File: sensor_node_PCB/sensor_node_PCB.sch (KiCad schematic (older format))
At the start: 32 parts, among them J1 USB_B_Mini, J3 OUTPUT_CONNECTOR, P1 BREAKOUTS, Q1 FDN340P, Q2 BSS138, Q3 BSS138, U1 LMV358IDGKR, U2 LD1117S50TR, U3 FT231XS, U4 LM1117-3.3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

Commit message: added dps310 to schem and board
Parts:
- added U?: dps310, symbol Kicad_symbols:dps310
- U9: symbol Kicad_symbols:sht20 -> sensor_node_PCB-rescue:sht20-Kicad_symbols
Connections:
- net 3V3_LDO: now also U9.~ (Vss), U?.6 (VDDIO), U?.8 (VDD); no longer U9.5 (VDD)
- net ARD_SCL_3V3: now also U9.~ (Vss), U?.4 (SCK); no longer U9.6 (SCL)
- net ARD_SDA_3V3: now also U9.~ (Vss), U?.3 (SDI); no longer U9.1 (SDA)
- net GND: now also U9.~ (Vss), U?.1 (GND), U?.7 (GND); no longer U9.2 (Vss)
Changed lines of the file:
@@
 	1350 1575 1675 1575
 $Comp
-L Kicad_symbols:sht20 U9
+L sensor_node_PCB-rescue:sht20-Kicad_symbols U9
 U 1 1 5FE5F04C
-P 7175 5275
-F 0 "U9" H 7000 5490 50  0000 C CNN
-F 1 "sht20" H 7000 5399 50  0000 C CNN
-F 2 "Package_DFN_QFN:DFN-6-1EP_3x3mm_P1mm_EP1.5x2.4mm" H 7175 5275 50  0001 C CNN
-F 3 "" H 7175 5275 50  0001 C CNN
-	1    7175 5275
+P 7275 5050
+F 0 "U9" H 7100 5355 50  0000 C CNN
+F 1 "sht20" H 7100 5264 50  0000 C CNN
+F 2 "Package_DFN_QFN:DFN-6-1EP_3x3mm_P1mm_EP1.5x2.4mm" H 7100 5173 50  0000 C CNN
+F 3 "" H 7275 5050 50  0001 C CNN
+	1    7275 5050
 	1    0    0    -1
 $EndComp
-Text Label 6500 5325 2    50   ~ 0
+Text Label 6600 5100 2    50   ~ 0
 ARD_SDA_3V3
-Text Label 7475 5325 0    50   ~ 0
+Text Label 7575 5100 0    50   ~ 0
 ARD_SCL_3V3
 $Comp
 L Arduino_Uno_R3_From_Scratch-rescue:3V3_LDO #PWR0113
 U 1 1 5FE707C4
-P 8050 5200
-F 0 "#PWR0113" H 8050 5160 30  0001 C CNN
-F 1 "3V3_LDO" H 8059 5338 30  0000 C CNN
-F 2 "" H 8050 5200 60  0000 C CNN
-F 3 "" H 8050 5200 60  0000 C CNN
-	1    8050 5200
+P 8150 4975
+F 0 "#PWR0113" H 8150 4935 30  0001 C CNN
+F 1 "3V3_LDO" H 8159 5113 30  0000 C CNN
+F 2 "" H 8150 4975 60  0000 C CNN
+F 3 "" H 8150 4975 60  0000 C CNN
+	1    8150 4975
 	1    0    0    -1
 $EndComp
@@
 L Arduino_Uno_R3_From_Scratch-rescue:GND #PWR0115
 U 1 1 5FE73051
-P 6425 5625
-F 0 "#PWR0115" H 6425 5375 50  0001 C CNN
-F 1 "GND" H 6430 5452 50  0000 C CNN
-F 2 "" H 6425 5625 60  0000 C CNN
-F 3 "" H 6425 5625 60  0000 C CNN
-	1    6425 5625
+P 6525 5400
+F 0 "#PWR0115" H 6525 5150 50  0001 C CNN
+F 1 "GND" H 6530 5227 50  0000 C CNN
+F 2 "" H 6525 5400 60  0000 C CNN
+F 3 "" H 6525 5400 60  0000 C CNN
+	1    6525 5400
 	1    0    0    -1
 $EndComp
 Wire Wire Line
-	6425 5625 6425 5425
+	6525 5400 6525 5200
 Wire Wire Line
-	6425 5425 6625 5425
+	6525 5200 6725 5200
 Wire Wire Line
-	7375 5325 7475 5325
+	7475 5100 7575 5100
 Wire Wire Line
-	6625 5325 6500 5325
+	6725 5100 6600 5100
 Wire Wire Line
-	8050 5200 8050 5425
+	8150 4975 8150 5200
 Wire Wire Line
-	8050 5425 7375 5425
+	8150 5200 7475 5200
+$Comp
+L Kicad_symbols:dps310 U?
+U 1 1 5FE12569
+P 7125 5925
+F 0 "U?" H 7125 6100 50  0000 C CNN
+F 1 "dps310" H 7125 6009 50  0000 C CNN
+F 2 "" H 7125 5925 50  0001 C CNN
+F 3 "" H 7125 5925 50  0001 C CNN
+	1    7125 5925
+	1    0    0    -1
+$EndComp
+$Comp
+L Arduino_Uno_R3_From_Scratch-rescue:GND #PWR?
+U 1 1 5FE1A61C
+P 6325 6000
+F 0 "#PWR?" H 6325 5750 50  0001 C CNN
+F 1 "GND" H 6330 5827 50  0000 C CNN
+F 2 "" H 6325 6000 60  0000 C CNN
+F 3 "" H 6325 6000 60  0000 C CNN
+	1    6325 6000
+	1    0    0    -1
+$EndComp
+Wire Wire Line
+	6325 6000 6325 5975
+Wire Wire Line
+	6325 5975 6675 5975
+$Comp
+L Arduino_Uno_R3_From_Scratch-rescue:GND #PWR?
+U 1 1 5FE23F96
+P 7875 6175
+F 0 "#PWR?" H 7875 5925 50  0001 C CNN
+F 1 "GND" H 7880 6002 50  0000 C CNN
+F 2 "" H 7875 6175 60  0000 C CNN
+F 3 "" H 7875 6175 60  0000 C CNN
+	1    7875 6175
+	0    -1   -1   0
+$EndComp
+Wire Wire Line
+	7575 6175 7875 6175
+$Comp
+L Arduino_Uno_R3_From_Scratch-rescue:3V3_LDO #PWR?
+U 1 1 5FE2D476
+P 8300 6000
+F 0 "#PWR?" H 8300 5960 30  0001 C CNN
+F 1 "3V3_LDO" H 8309 6138 30  0000 C CNN
+F 2 "" H 8300 6000 60  0000 C CNN
+F 3 "" H 8300 6000 60  0000 C CNN
+	1    8300 6000
+	1    0    0    -1
+$EndComp
+Wire Wire Line
+	7575 6275 8300 6275
+Wire Wire Line
+	7575 6075 8300 6075
+Wire Wire Line
+	8300 6075 8300 6000
+Wire Wire Line
+	8300 6075 8300 6275
+Connection ~ 8300 6075
+Text Label 6250 6400 2    50   ~ 0
+ARD_SDA_3V3
+Text Label 6250 6525 2    50   ~ 0
+ARD_SCL_3V3
+Wire Wire Line
+	6250 6400 6500 6400
+Wire Wire Line
+	6500 6400 6500 6175
+Wire Wire Line
+	6500 6175 6675 6175
+Wire Wire Line
+	6250 6525 6575 6525
+Wire Wire Line
+	6575 6525 6575 6275
+Wire Wire Line
+	6575 6275 6675 6275
 $EndSCHEMATC

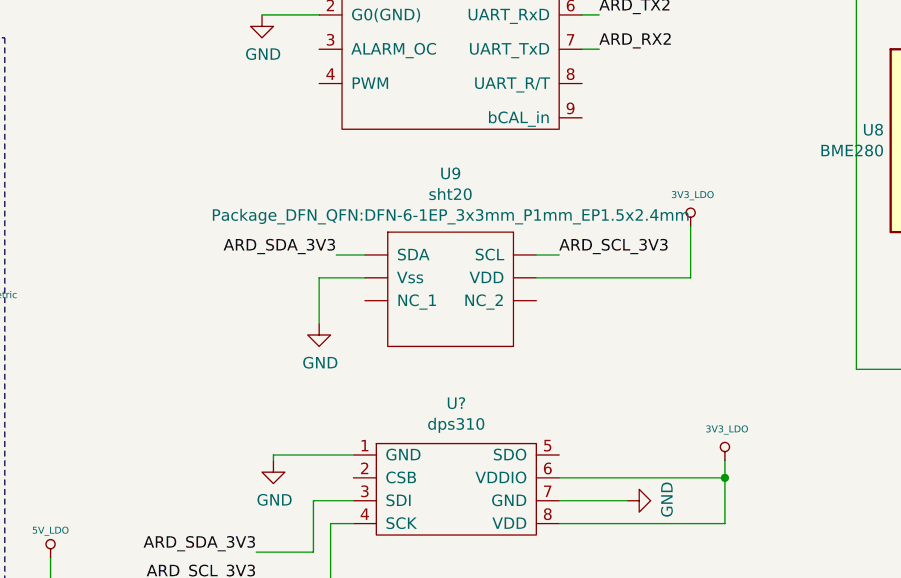
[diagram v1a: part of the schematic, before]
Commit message: changed term block to 5.08mm - added silk pin labels
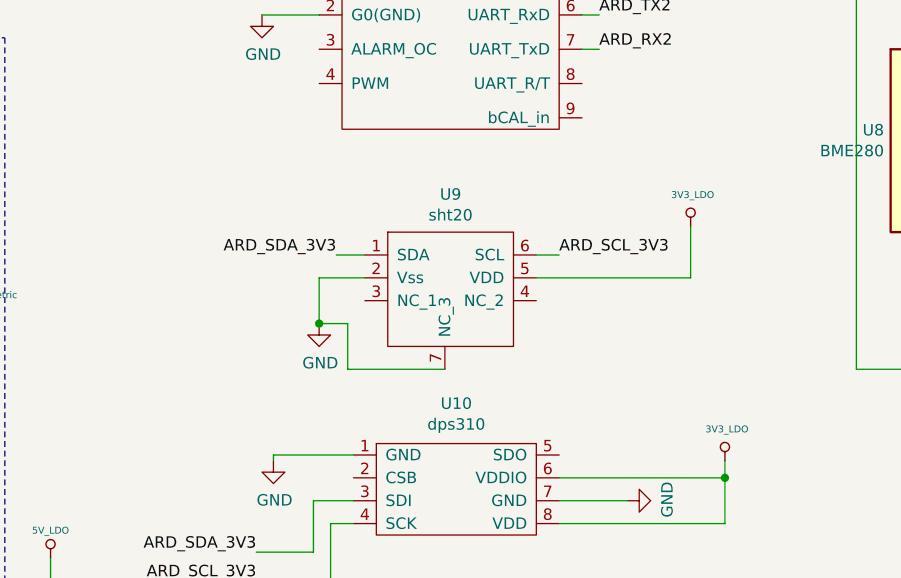
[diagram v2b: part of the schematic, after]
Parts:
- removed U9: sht20, Package_DFN_QFN:DFN-6-1EP_3x3mm_P1mm_EP1.5x2.4mm, symbol sensor_node_PCB-rescue:sht20-Kicad_symbols
- added U9: sht20, Package_DFN_QFN:DFN-6-1EP_3x3mm_P1mm_EP1.5x2.4mm, symbol Kicad_symbols:sht20
- U10: renamed from U?; footprint (none) -> Package_LGA:Bosch_LGA-8_2x2.5mm_P0.65mm_ClockwisePinNumbering
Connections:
- net 3V3_LDO: now also U9.5 (VDD)
- net ARD_SCL_3V3: now also U9.6 (SCL)
- net ARD_SDA_3V3: now also U9.1 (SDA)
- net GND: now also U9.2 (Vss), U9.7 (NC_3)
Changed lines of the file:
@@
 Wire Wire Line
 	1350 1575 1675 1575
-$Comp
-L sensor_node_PCB-rescue:sht20-Kicad_symbols U9
-U 1 1 5FE5F04C
-P 7275 5050
-F 0 "U9" H 7100 5355 50  0000 C CNN
-F 1 "sht20" H 7100 5264 50  0000 C CNN
-F 2 "Package_DFN_QFN:DFN-6-1EP_3x3mm_P1mm_EP1.5x2.4mm" H 7100 5173 50  0000 C CNN
-F 3 "" H 7275 5050 50  0001 C CNN
-	1    7275 5050
-	1    0    0    -1
-$EndComp
 Text Label 6600 5100 2    50   ~ 0
 ARD_SDA_3V3
@@
 	8150 5200 7475 5200
 $Comp
-L Kicad_symbols:dps310 U?
+L Kicad_symbols:dps310 U10
 U 1 1 5FE12569
 P 7125 5925
-F 0 "U?" H 7125 6100 50  0000 C CNN
+F 0 "U10" H 7125 6100 50  0000 C CNN
 F 1 "dps310" H 7125 6009 50  0000 C CNN
-F 2 "" H 7125 5925 50  0001 C CNN
+F 2 "Package_LGA:Bosch_LGA-8_2x2.5mm_P0.65mm_ClockwisePinNumbering" H 7125 5925 50  0001 C CNN
 F 3 "" H 7125 5925 50  0001 C CNN
 	1    7125 5925
@@
 $EndComp
 $Comp
-L Arduino_Uno_R3_From_Scratch-rescue:GND #PWR?
+L Arduino_Uno_R3_From_Scratch-rescue:GND #PWR0143
 U 1 1 5FE1A61C
 P 6325 6000
-F 0 "#PWR?" H 6325 5750 50  0001 C CNN
+F 0 "#PWR0143" H 6325 5750 50  0001 C CNN
 F 1 "GND" H 6330 5827 50  0000 C CNN
 F 2 "" H 6325 6000 60  0000 C CNN
@@
 	6325 5975 6675 5975
 $Comp
-L Arduino_Uno_R3_From_Scratch-rescue:GND #PWR?
+L Arduino_Uno_R3_From_Scratch-rescue:GND #PWR0144
 U 1 1 5FE23F96
 P 7875 6175
-F 0 "#PWR?" H 7875 5925 50  0001 C CNN
+F 0 "#PWR0144" H 7875 5925 50  0001 C CNN
 F 1 "GND" H 7880 6002 50  0000 C CNN
 F 2 "" H 7875 6175 60  0000 C CNN
@@
 	7575 6175 7875 6175
 $Comp
-L Arduino_Uno_R3_From_Scratch-rescue:3V3_LDO #PWR?
+L Arduino_Uno_R3_From_Scratch-rescue:3V3_LDO #PWR0145
 U 1 1 5FE2D476
 P 8300 6000
-F 0 "#PWR?" H 8300 5960 30  0001 C CNN
+F 0 "#PWR0145" H 8300 5960 30  0001 C CNN
 F 1 "3V3_LDO" H 8309 6138 30  0000 C CNN
 F 2 "" H 8300 6000 60  0000 C CNN
@@
 Wire Wire Line
 	6575 6275 6675 6275
+$Comp
+L Kicad_symbols:sht20 U9
+U 1 1 5FE623C8
+P 7275 5050
+F 0 "U9" H 7100 5265 50  0000 C CNN
+F 1 "sht20" H 7100 5174 50  0000 C CNN
+F 2 "Package_DFN_QFN:DFN-6-1EP_3x3mm_P1mm_EP1.5x2.4mm" H 7275 5050 50  0001 C CNN
+F 3 "" H 7275 5050 50  0001 C CNN
+	1    7275 5050
+	1    0    0    -1
+$EndComp
+Wire Wire Line
+	7075 5600 6650 5600
+Wire Wire Line
+	6650 5600 6650 5400
+Wire Wire Line
+	6650 5400 6525 5400
+Connection ~ 6525 5400
 $EndSCHEMATC
